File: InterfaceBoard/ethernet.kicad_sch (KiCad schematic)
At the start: 40 parts, among them P1 RB1-125BAG1A, U1 W5500, Y1 25 MHz

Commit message: InterfaceBoard: Add RS-232/DE-9
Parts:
- JP1, JP2, JP3: footprint Jumper:SolderJumper-2_P1.3mm_Open_TrianglePad1.0x1.5mm -> lib:0603_solder_jumper
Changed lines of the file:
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@@
     (property "Reference" "JP1" (id 0) (at 58.42 60.96 0))
     (property "Value" "PMODE0" (id 1) (at 49.53 60.96 0))
-    (property "Footprint" "Jumper:SolderJumper-2_P1.3mm_Open_TrianglePad1.0x1.5mm" (id 2) (at 54.61 62.23 0)
+    (property "Footprint" "lib:0603_solder_jumper" (id 2) (at 54.61 62.23 0)
       (effects (font (size 1.27 1.27)) hide)
     )
@@
     (property "Reference" "JP2" (id 0) (at 58.42 64.77 0))
     (property "Value" "PMODE1" (id 1) (at 49.53 64.77 0))
-    (property "Footprint" "Jumper:SolderJumper-2_P1.3mm_Open_TrianglePad1.0x1.5mm" (id 2) (at 54.61 66.04 0)
+    (property "Footprint" "lib:0603_solder_jumper" (id 2) (at 54.61 66.04 0)
       (effects (font (size 1.27 1.27)) hide)
     )
@@
     (property "Reference" "JP3" (id 0) (at 58.42 68.58 0))
     (property "Value" "PMODE2" (id 1) (at 49.53 68.58 0))
-    (property "Footprint" "Jumper:SolderJumper-2_P1.3mm_Open_TrianglePad1.0x1.5mm" (id 2) (at 54.61 69.85 0)
+    (property "Footprint" "lib:0603_solder_jumper" (id 2) (at 54.61 69.85 0)
       (effects (font (size 1.27 1.27)) hide)
     )

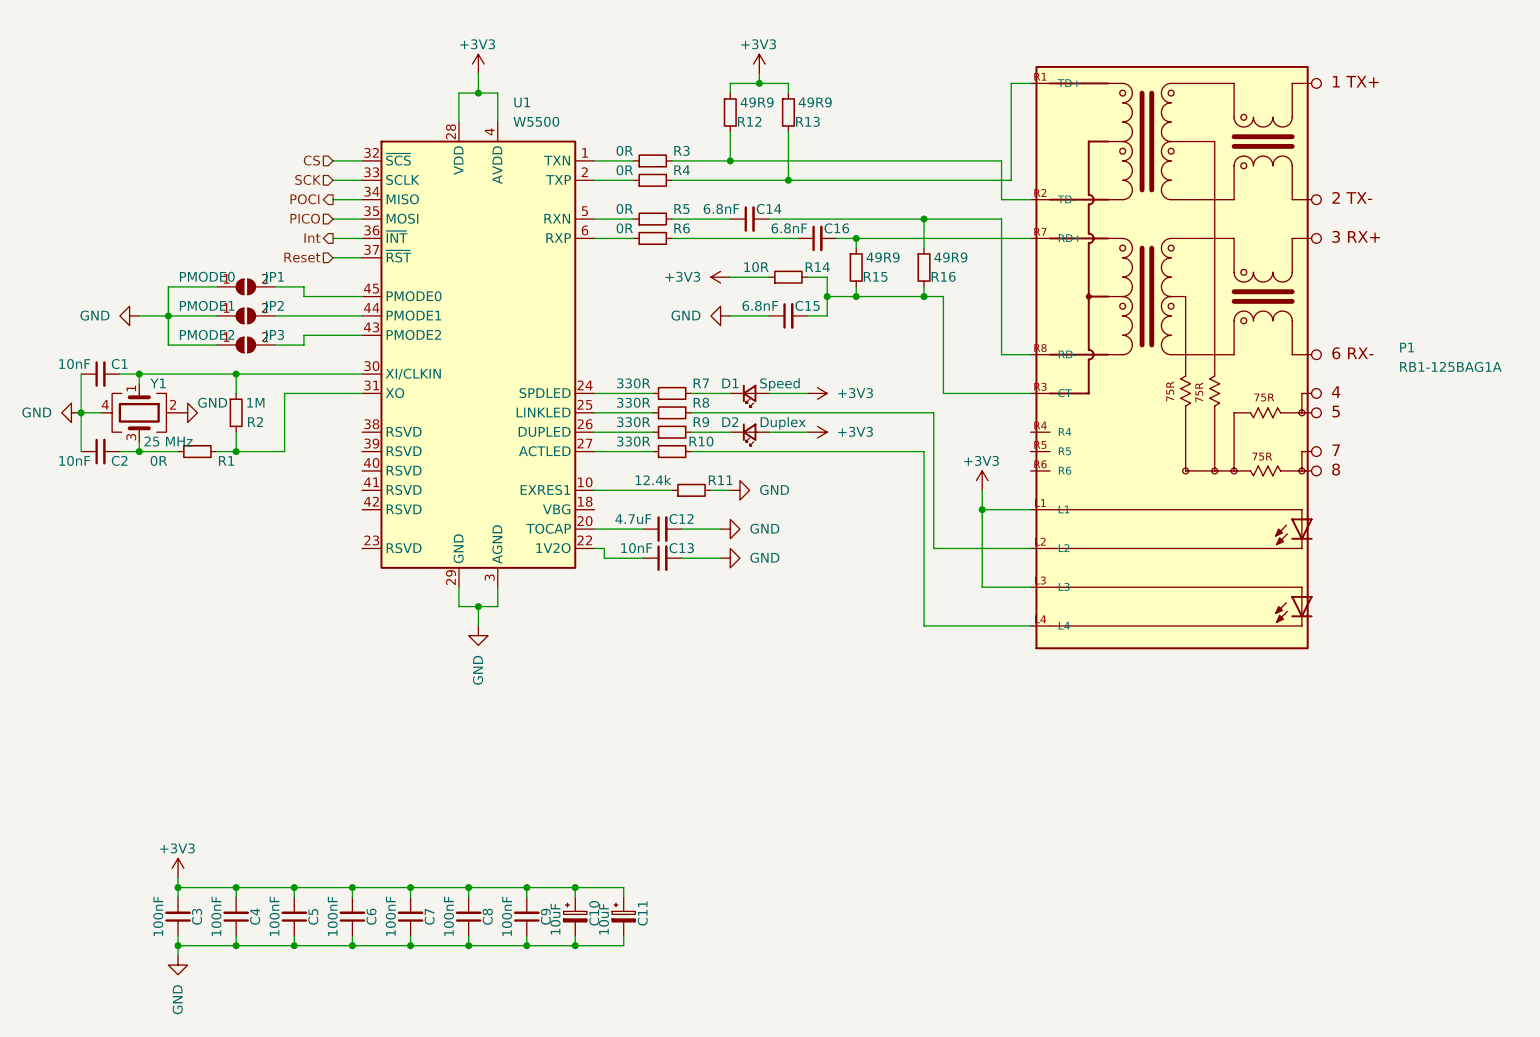
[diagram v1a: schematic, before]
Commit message: InterfaceBoard: Add STM32G0B1RET
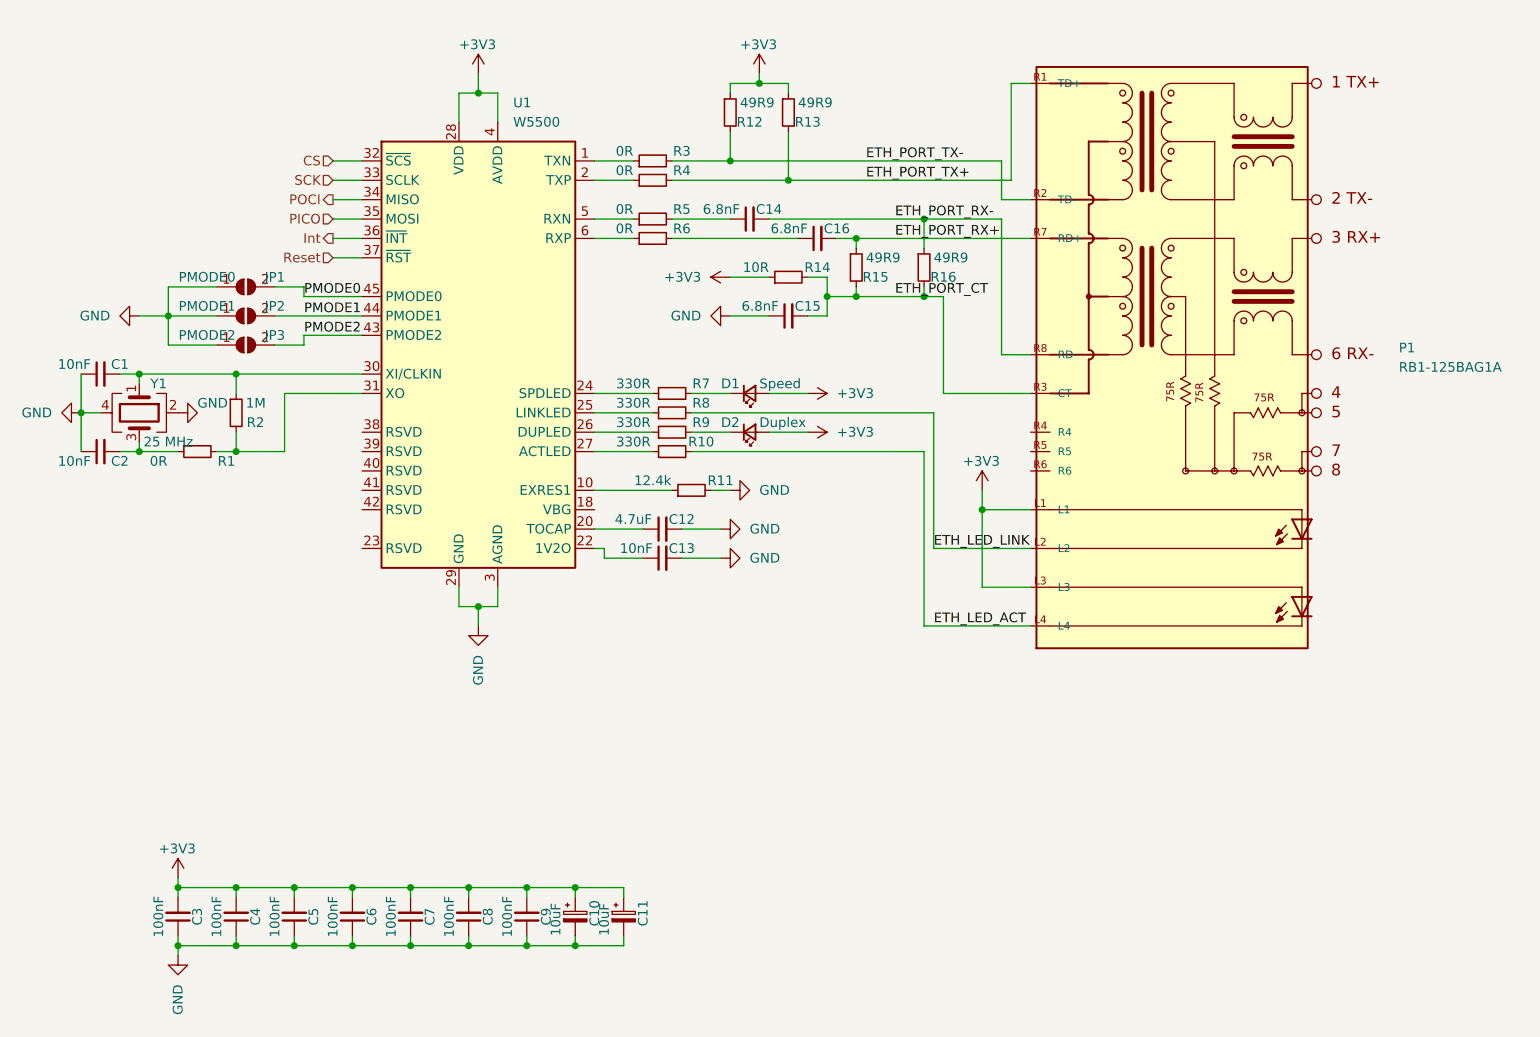
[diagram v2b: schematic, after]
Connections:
- net ETH_PORT_TX-: now reaches P1.R2 (TD-), R12.2, R3.2
- net ETH_PORT_RX-: now reaches C14.2, P1.R8 (RD-), R16.1
- net ETH_PORT_RX+: now reaches C16.2, P1.R7 (RD+), R15.1
- net ETH_PORT_CT: now reaches C15.2, P1.R3 (CT), R14.2, R15.2, R16.2
- net ETH_PORT_TX+: now reaches P1.R1 (TD+), R13.2, R4.2
- net PMODE0: now reaches JP1.2 (B), U1.45 (PMODE0)
- net PMODE1: now reaches JP2.2 (B), U1.44 (PMODE1)
- net PMODE2: now reaches JP3.2 (B), U1.43 (PMODE2)
- net ETH_LED_LINK: now reaches P1.L2, R8.2
- net ETH_LED_ACT: now reaches P1.L4, R10.2
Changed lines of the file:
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@@
     (stroke (width 0) (type default) (color 0 0 0 0))
+  )
+  (label "ETH_PORT_CT" (at 139.7 63.5 0)
+    (effects (font (size 1.27 1.27)) (justify left bottom))
+  )
+  (label "ETH_PORT_RX+" (at 139.7 55.88 0)
+    (effects (font (size 1.27 1.27)) (justify left bottom))
+  )
+  (label "ETH_LED_LINK" (at 144.78 96.52 0)
+    (effects (font (size 1.27 1.27)) (justify left bottom))
+  )
+  (label "ETH_LED_ACT" (at 144.78 106.68 0)
+    (effects (font (size 1.27 1.27)) (justify left bottom))
+  )
+  (label "ETH_PORT_RX-" (at 139.7 53.34 0)
+    (effects (font (size 1.27 1.27)) (justify left bottom))
+  )
+  (label "ETH_PORT_TX-" (at 135.89 45.72 0)
+    (effects (font (size 1.27 1.27)) (justify left bottom))
+  )
+  (label "PMODE1" (at 62.23 66.04 0)
+    (effects (font (size 1.27 1.27)) (justify left bottom))
+  )
+  (label "PMODE2" (at 62.23 68.58 0)
+    (effects (font (size 1.27 1.27)) (justify left bottom))
+  )
+  (label "PMODE0" (at 62.23 63.5 0)
+    (effects (font (size 1.27 1.27)) (justify left bottom))
+  )
+  (label "ETH_PORT_TX+" (at 135.89 48.26 0)
+    (effects (font (size 1.27 1.27)) (justify left bottom))
   )
   (hierarchical_label "POCI" (shape output) (at 66.04 50.8 180)

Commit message: InterfaceBoard: Add 3.3 V regulater, test points.
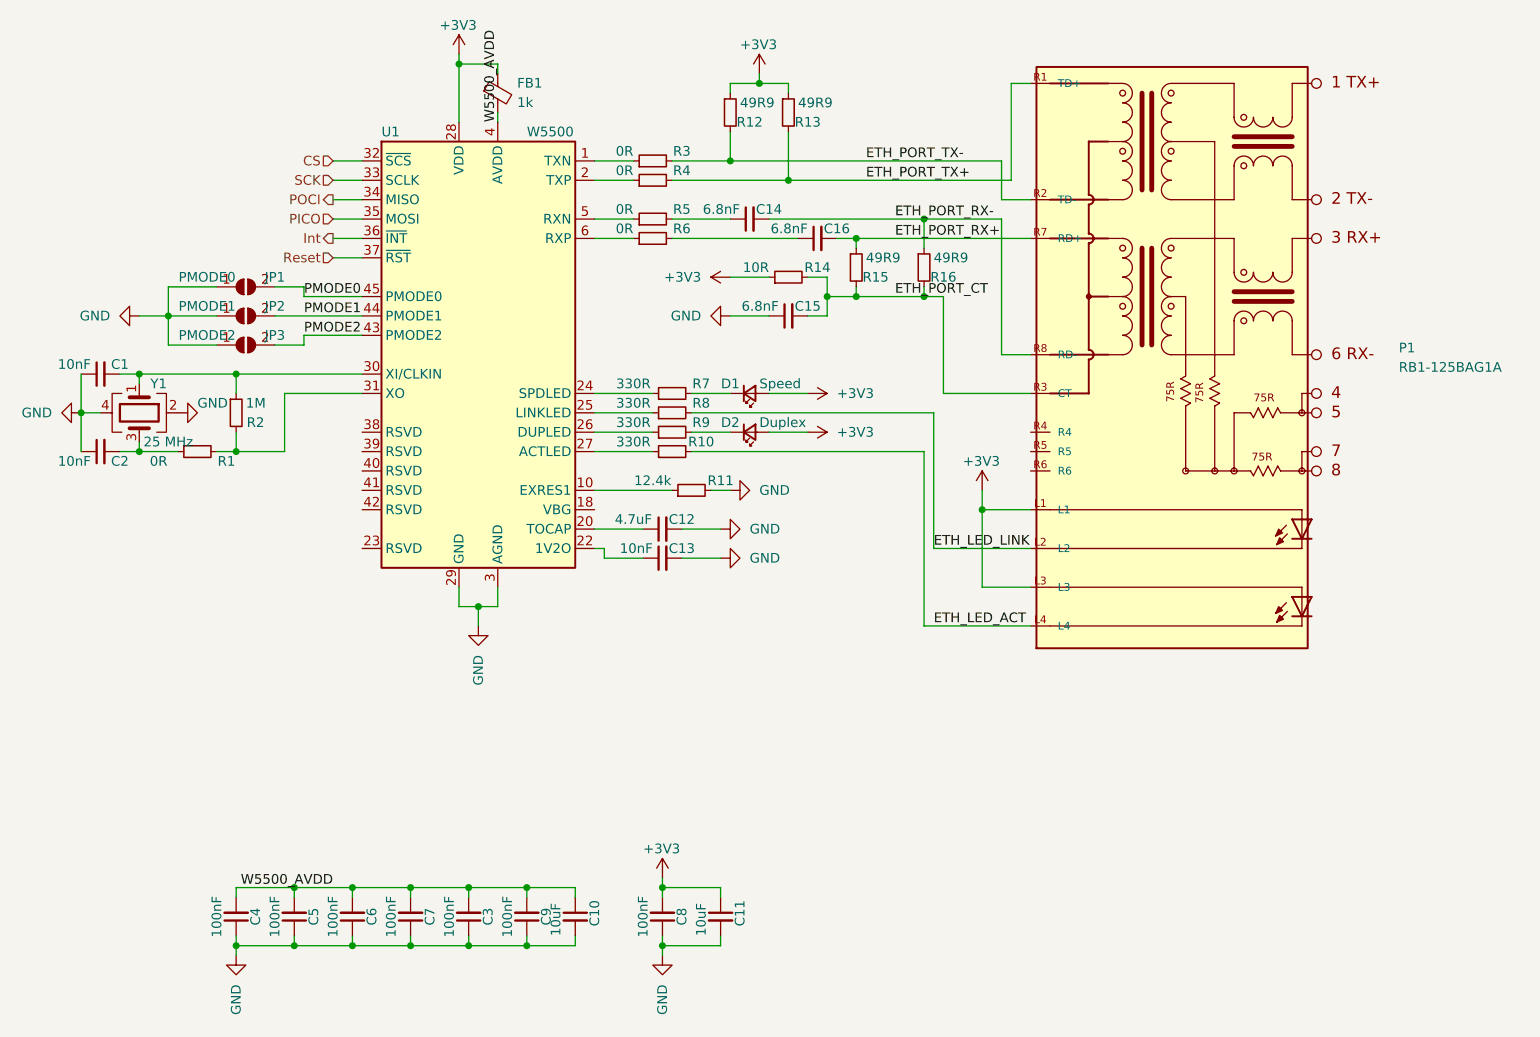
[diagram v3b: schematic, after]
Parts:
- added FB1: 1k, Inductor_SMD:L_0805_2012Metric, symbol Device:FerriteBead_Small
- C10, C11: footprint Capacitor_SMD:CP_Elec_5x5.9 -> Capacitor_SMD:C_0805_2012Metric; symbol Device:C_Polarized_Small -> Device:C_Small; DigiKey (none) -> https://www.digikey.com/en/products/detail/samsung-electro-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
- U1: DigiKey (none) -> https://www.digikey.com/en/products/detail/wiznet/W5500/442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
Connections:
- net +3V3: now also FB1.1; no longer C10.1, C3.2, C4.2, C5.2, C6.2, C7.2, C9.2, U1.11 (AVDD), U1.15 (AVDD), U1.17 (AVDD), U1.21 (AVDD), U1.4 (AVDD), U1.8 (AVDD)
- new net W5500_AVDD: C10.1, C3.2, C4.2, C5.2, C6.2, C7.2, C9.2, FB1.2, U1.11 (AVDD), U1.15 (AVDD), U1.17 (AVDD), U1.21 (AVDD), U1.4 (AVDD), U1.8 (AVDD)
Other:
- moved on the sheet: C3, C8

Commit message: InterfaceBoard: Rev 1.0
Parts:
- renumbered C10 to C1, C13 to C2, C6 to C22, C4 to C23, C9 to C24, C3 to C25, C8 to C26, C5 to C27, C7 to C28, C15 to C29, C12 to C3, C11 to C4, C1 to C5, C16 to C6, C14 to C7, C2 to C8, D2 to D1, D1 to D2, R11 to R1, R9 to R15, R7 to R17, R6 to R2, R5 to R3, R2 to R4, R4 to R5, R3 to R6, R1 to R7, R12 to R8, R8 to R81, R16 to R82, R15 to R83, R10 to R84, R14 to R85, R13 to R9
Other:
- company: (none) -> Peter Farley
- title: (none) -> Kiethley 615 Interface Board

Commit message: InterfaceBoard: Add BOM
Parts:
- C2, C29, C5, C6, C7, C8, R4: DigiKey (none) -> https://www.digikey.com/en/products/detail/walsin-technolog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
- C22, C23, C24, C25, C26, C27, C28, C3: DigiKey (none) -> https://www.digikey.com/en/products/detail/samsung-electro-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
- D1, D2: DigiKey (none) -> https://www.digikey.com/en/products/detail/harvatek-corpora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
- JP1, JP2, JP3: now left out of the parts list
- P1: DigiKey (none) -> https://www.digikey.com/en/products/detail/wiznet/RB1-125BA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
- R1: DigiKey (none) -> https://www.digikey.com/en/products/detail/stackpole-electr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
- R15, R17, R81, R84: value 330R -> 330; DigiKey (none) -> https://www.digikey.com/en/products/detail/walsin-technolog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
- R2, R3, R5, R6, R7: value 0R -> 0; DigiKey (none) -> https://www.digikey.com/en/products/detail/walsin-technolog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
- R8, R82, R83, R9: value 49R9 -> 49.9; DigiKey (none) -> https://www.digikey.com/en/products/detail/stackpole-electr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
- R85: value 10R -> 10; DigiKey (none) -> https://www.digikey.com/en/products/detail/walsin-technolog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
- Y1: DigiKey (none) -> https://www.digikey.com/en/products/detail/raltron-electron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
